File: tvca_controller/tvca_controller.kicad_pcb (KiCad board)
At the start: 2 copper layers, 84.3 x 59.2 mm, 57 parts, among them J1 Programming Header, J2 PT 1,5/ 4-5,0-H, J3 4DB-P108-02, J4 PT 1,5/ 4-5,0-H, J5 4DB-P108-02, J6 PT 1,5/ 4-5,0-H, J7 4DB-P108-02, J9 4DB-P108-02, U1 PIC18F26K83, U2 MCP2562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

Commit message: Address routing comments
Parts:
- moved Y1 0.48 mm to (140.4, 108.8)
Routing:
- net GND: track 2.77 -> 20.9 mm, vias 2 -> 0
- net /CUR_1: track 68.0 -> 60.4 mm, vias 1 -> 2
- net Net-(U9-SEL_0): track 25.9 -> 30.3 mm, vias 0 -> 2
- net +5V: track 157.8 -> 153.6 mm, vias 3 -> 4
- net Net-(U9-PWM): track 21.4 -> 25.5 mm, vias 0 -> 2
- net /CUR_2: track 73.2 -> 75.9 mm
- net /ENCDRA_2: track 39.0 -> 41.2 mm
- net Net-(U8-CS): track 34.1 -> 32.4 mm
- net /VBAT_1: track 22.9 -> 24.5 mm, vias 0 -> 2
- net /CUR_AMP: track 36.7 -> 35.4 mm
- net /SEL_1: track 12.8 -> 11.8 mm
- net Net-(U9-CS): track 32.9 -> 32.3 mm
- net Net-(U3-IN+): track 12.1 -> 12.6 mm, vias 0 -> 2

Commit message: Various small fixes
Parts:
- R12, R13: moved to B.Cu
- moved R13 33.4 mm to (142.9, 123.2)
- moved R12 27.3 mm to (142.9, 120.2)
- moved C13 12.9 mm to (186.9, 104.2), turned to 90 degrees
- moved C12 12.8 mm to (107.3, 104.4), turned to -90 degrees
- moved R16 2.34 mm to (161.1, 117.6)
- moved C5 2.11 mm to (152.5, 103.0), turned to 90 degrees
- moved J5 0.52 mm to (166.2, 123.5)
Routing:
- net /VBAT_2: track 40.0 -> 11.8 mm, vias 0 -> 1
- net +5V: track 153.6 -> 177.3 mm
- net Net-(U8-PWM): track 21.3 -> 24.8 mm, vias 0 -> 2
- net /Motor_2/POWER: track 18.6 -> 21.9 mm
- net Net-(U8-CS): track 32.4 -> 35.6 mm
- net /CLW_2: track 15.8 -> 13.0 mm
- net /CUR_1: track 60.4 -> 62.4 mm
- net Net-(U3-IN+): track 12.6 -> 10.7 mm
- net /CCW_2: track 15.6 -> 17.0 mm
- net GND: track 20.9 -> 21.9 mm, vias 0 -> 5
- net Net-(U8-IN_B): track 6.91 -> 7.89 mm, vias 0 -> 2
- net /PWM_1: track 8.73 -> 7.76 mm
- net /~{MCLR}: track 18.3 -> 19.3 mm, vias 2 -> 0
- net /CUR_AMP: track 35.4 -> 34.5 mm, vias 2 -> 1
- net Net-(U9-CS): track 32.3 -> 31.6 mm
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
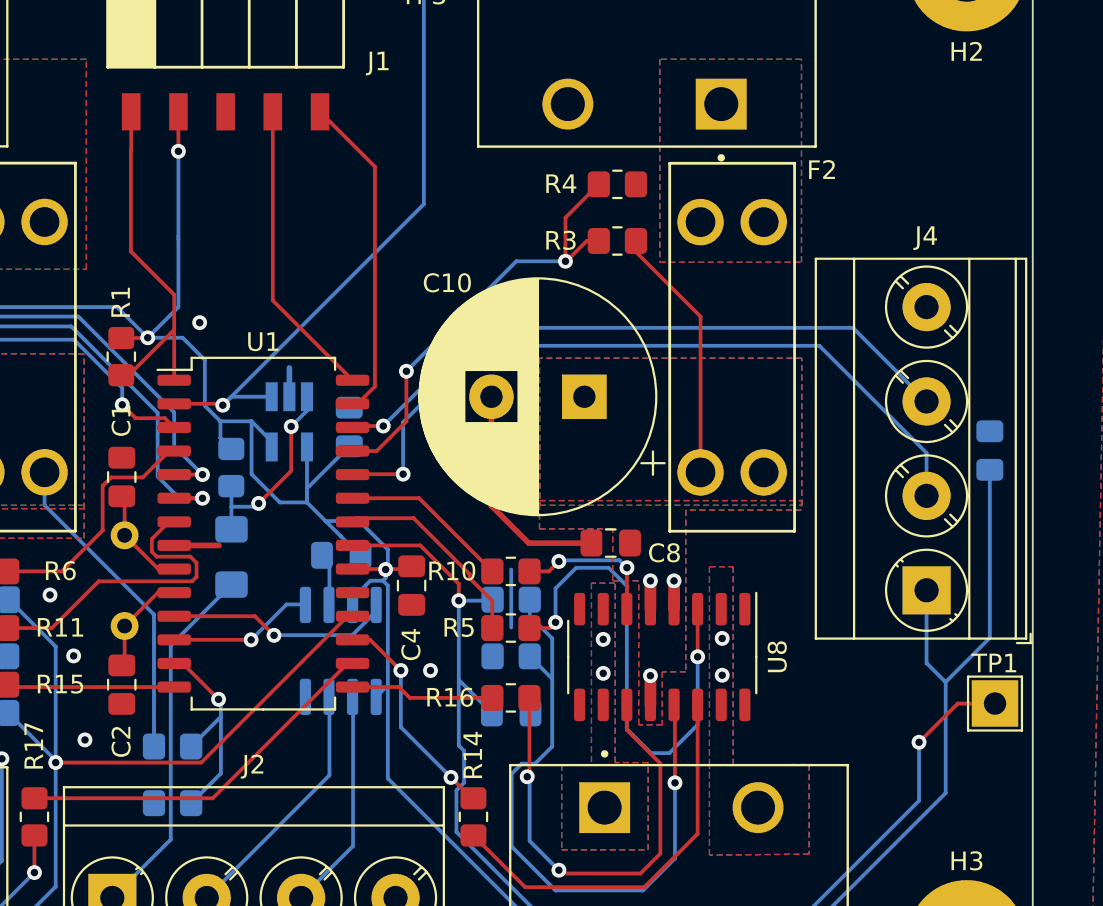
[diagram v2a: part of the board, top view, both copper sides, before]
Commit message: Add team logo, a bunch of lables, and my name
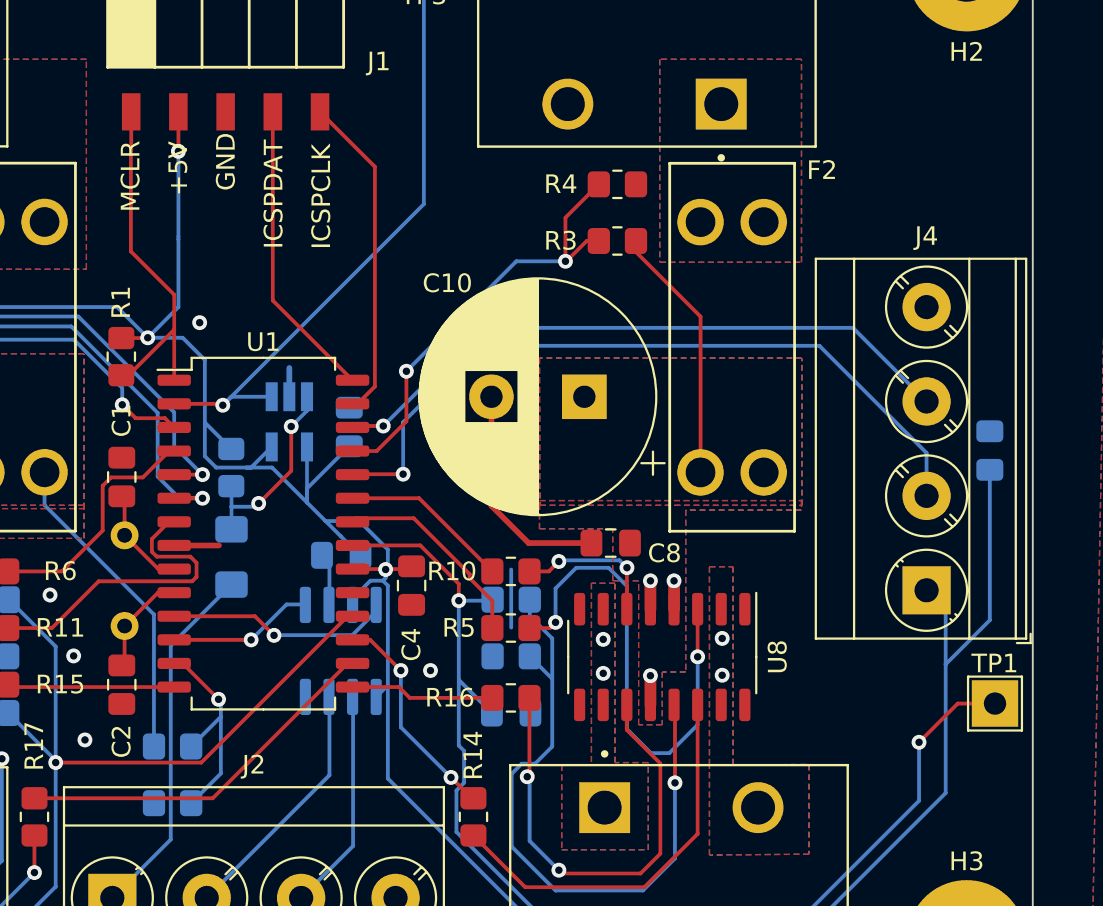
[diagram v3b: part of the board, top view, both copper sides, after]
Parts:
- added G***: LOGO, TeamLogo:Logo_SilkScreen_15mm, B.Cu at (147.1, 81.7)
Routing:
- net +5V: track 177.3 -> 176.4 mm
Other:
- board text added: "+5V"
- board text added: "1"
- board text added: "2"
- board text added: "A1"
- board text added: "A2"
- board text added: "B1"
- board text added: "B2"
- board text added: "CANH"
- board text added: "CANL"
- board text added: "Designed by Kavin Satheeskumar"
- board text added: "GND"
- board text added: "ICSPCLK"
- board text added: "ICSPDAT"
- board text added: "MCLR"
- board text added: "POWER"
